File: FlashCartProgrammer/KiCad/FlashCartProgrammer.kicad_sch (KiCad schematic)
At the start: 85 parts, among them J1 Vic20 Cartridge Connector, J10 Vic20 Header, J11 ZIF Header, J2 C64 Cartridge Connector, J3 +5V, J4 USB_A_KeyBoard, J5 BOOT SEL, J6 VGA, J7 DM3D-SF, J8 SWD, J9 C64 Header, U1 TLV74311PDBVR, U10 27C400, U2 TLV74333PDBVR, U3 W25Q16JVSSIQ, U4 RP2350B-QFN80, U5 74LS573, U6 74LS573, U7 TXS0108EPW, U8 TXS0108EPW, U9 TXS0108EPW, Y1 12MHz

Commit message: - Cleaned up the Flash Cart Programmer PCB a bit.
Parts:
- removed C15: 4.7uf, Capacitor_SMD:C_0603_1608Metric, symbol Device:C_Small
- removed C31: 100nf, Capacitor_SMD:C_0603_1608Metric, symbol Device:C_Small
- removed J1: Vic20 Cartridge Connector, SamacSys_Parts:307044558201, symbol SamacSys_Parts:307-044-558-201
- removed J2: C64 Cartridge Connector, SamacSys_Parts:395044524202, symbol SamacSys_Parts:395-044-524-202
- removed J6: VGA, SamacSys_Parts:117345301, symbol Connector:DE15_Socket_HighDensity_MountingHoles
- removed U9: TXS0108EPW, Package_SO:TSSOP-20_4.4x6.5mm_P0.65mm, symbol Logic_LevelTranslator:TXS0108EPW
- added J1: Vic20_Cartridge_Connector, _Custom:Vic20-Cartridge-Connector, symbol _Custom:Vic20_Cartridge_Connector
- added J2: c64-Cartridge-Connector, _Custom:c64-Cartridge-Connector, symbol _Custom:c64-Cartridge-Connector
- added J6: DE15_Socket_HighDensity_MountingHoles, _Custom:DSUB-15, symbol _Custom:DE15_Socket_HighDensity_MountingHoles
- added R25, R26: 10k, Resistor_SMD:R_0603_1608Metric, symbol Device:R_Small
- added U18: 74LS245, Package_SO:TSSOP-20_4.4x6.5mm_P0.65mm, symbol Dave:74LVC245A
- C22, C23: value 8pf -> 12pf
- J11: footprint Connector_PinHeader_2.54mm:PinHeader_1x03_P2.54mm_Vertical -> Connector_PinHeader_2.54mm:PinHeader_1x04_P2.54mm_Vertical; symbol Connector:Conn_01x03_Pin -> Connector:Conn_01x04_Pin
- J4: footprint Connector_USB:USB_A_Connfly_DS1095 -> _Custom:USB_A
- R1, R2, R3, R4, R5, R7, R8, R9: value 27 -> 27R
- R10, R12, R14: value 340 -> 330R
- U10: footprint Socket:DIP_Socket-40_W11.9mm_W12.7mm_W15.24mm_W17.78mm_W18.5mm_3M_240-1280-00-0602J -> _Custom:ZIF-40_W11.9_W12.7_W15.24_W17.78_W18.5_3M_240-1280-00-0602J
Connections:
- net +3V3: no longer C30.2, R24.2
- net +5V: now also C30.2, J1.21 (5V), J2.2 (5V=), J2.3 (5V), U18.20 (VCC)
- net 3v3_A16: now also U18.18 (B0)
- net 3v3_A17: now also U18.17 (B1)
- net 3v3_A18: now also U18.16 (B2)
- net 3v3_A19: now also U18.15 (B3)
- net A0: now also J1.B (A0), J2.Y (A0)
- net A1: now also J1.C (A1), J2.X (A1)
- net A10: now also J1.N (A10), J2.M (A10)
- net A11: now also J1.P (A11), J2.L (A11)
- net A12: now also J1.R (A12), J2.K (A12)
- net A13: now also J2.11 (~{ROML})
- net A16: now also U18.2 (A0)
- net A17: now also U18.3 (A1)
- net A18: now also U18.4 (A2)
- net A19: now also U18.5 (A3)
- net A2: now also J1.D (A2), J2.W (A2)
- net A3: now also J1.E (A3), J2.V (A3)
- net A4: now also J1.F (A4), J2.U (A4)
- net A5: now also J1.H (A5), J2.T (A5)
- net A6: now also J1.J (A6), J2.S (A6)
- net A7: now also J1.K (A7), J2.R (A7)
- net A8: now also J1.L (A8), J2.P (A8)
- net A9: now also J1.M (A9), J2.N (A9)
- net D0: now also J1.2 (D0), J2.21 (D0)
- net D1: now also J1.3 (D1), J2.20 (D1)
- net D2: now also J1.4 (D2), J2.19 (D2)
- net D3: now also J1.5 (D3), J2.18 (D3)
- net D4: now also J1.6 (D4), J2.17 (D4)
- net D5: now also J1.7 (D5), J2.16 (D5)
- net D6: now also J1.8 (D6), J2.15 (D6)
- net D7: now also J1.9 (D7), J2.14 (D7)
- net GND: now also R24.2, J1.1 (GND1), J1.22 (GND2), J1.A (GND3), J1.Z (GND4), J2.0 (MH), J2.1 (GND1), J2.22 (GND2), J2.A (GND4), J2.Z (GND3), J6.10, J6.5, J6.6, J6.7, J6.8, J6.SH, R25.2, R26.1, U18.10 (GND)
- net VGA_BLUE: now also J6.3
- net VGA_GREEN: now also J6.2
- net VGA_H_SYNC: now also J6.13
- net VGA_RED: now also J6.1
- net VGA_V_SYNC: now also J6.14
- net ~{3v3_BYTE}: now also U18.14 (B4)
- net ~{3v3_OE}: now also U18.12 (B6)
- net ~{3v3_WE}: now also U18.13 (B5)
- net ~{BYTE}: now also U18.6 (A4)
- net ~{OE}: now also U18.8 (A6)
- net ~{WE}: now also U18.7 (A5)
- net at R4.1: now also J1.13 (~{BLK5})
- net at R24.1: now also U18.1 (A->B)
- net at R1.1: now also J1.10 (~{BLK1})
- net at R2.1: now also J1.11 (~{BLK2})
- net at R3.1: now also J1.12 (~{BLK3})
- net at R5.2: now also J2.B (~{ROMH})
- net SPI1.CS renamed SPI1.~{CS}
- net ~{3v3_CE} renamed ~{3v3_RESET}
- net ~{3v3_RESET}: now also U18.11 (B7)
- net ~{CE}: no longer names the net of U10.10 (~{CE})
- net ~{CE}: now also R26.2
- new net: R25.1, U18.19 (CE)
- new net ~{RESET}: J11.4 (Pin_4), U18.9 (A7)
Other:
- moved on the sheet: C24, C25, U5, U6

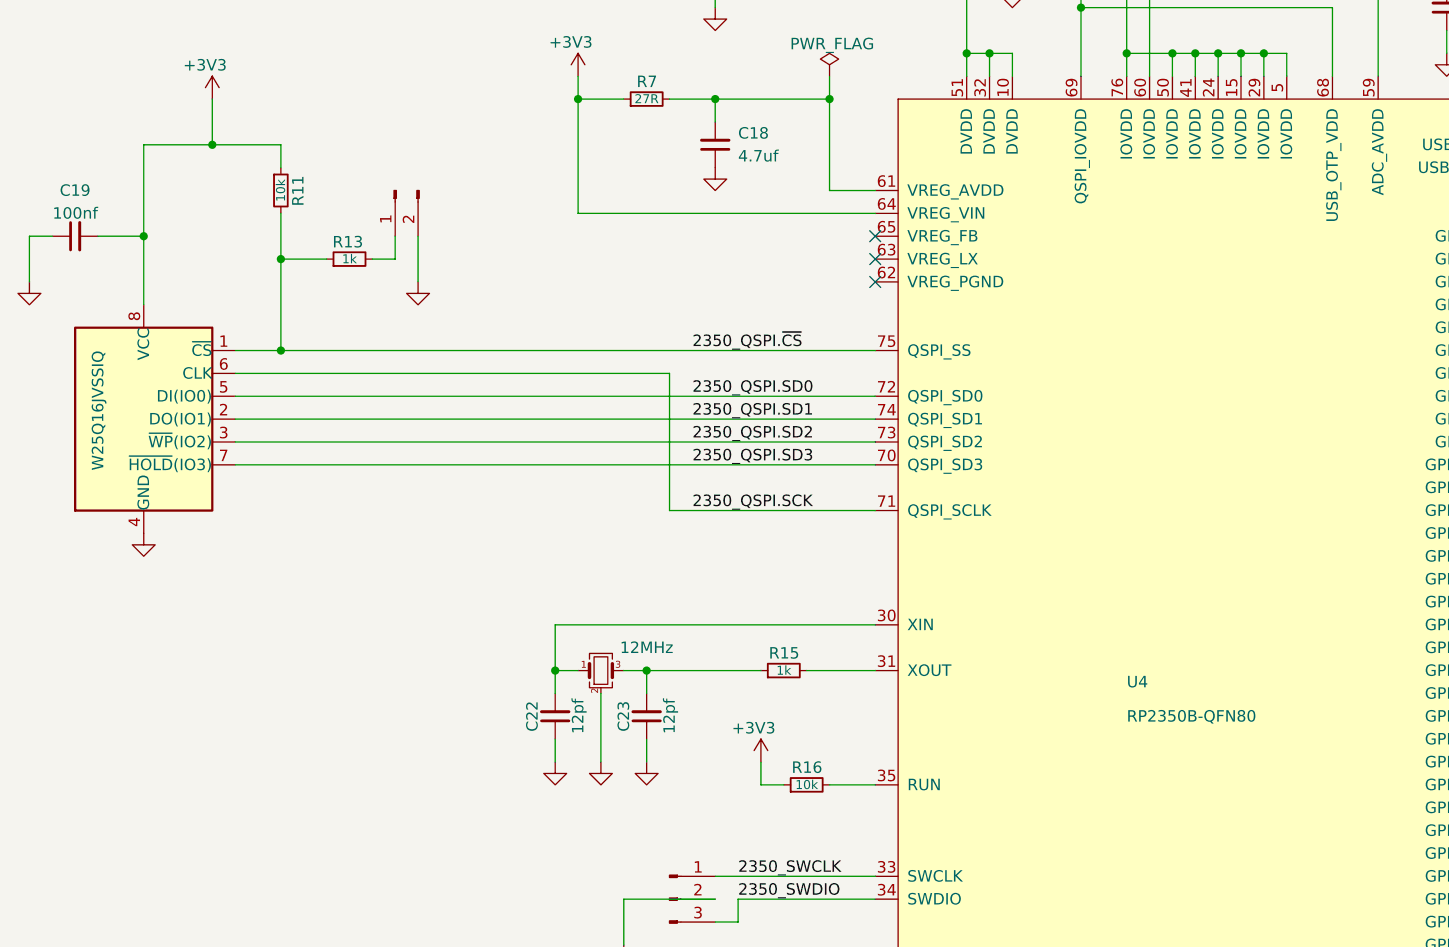
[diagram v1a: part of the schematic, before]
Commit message: - Removed references to my local parts.
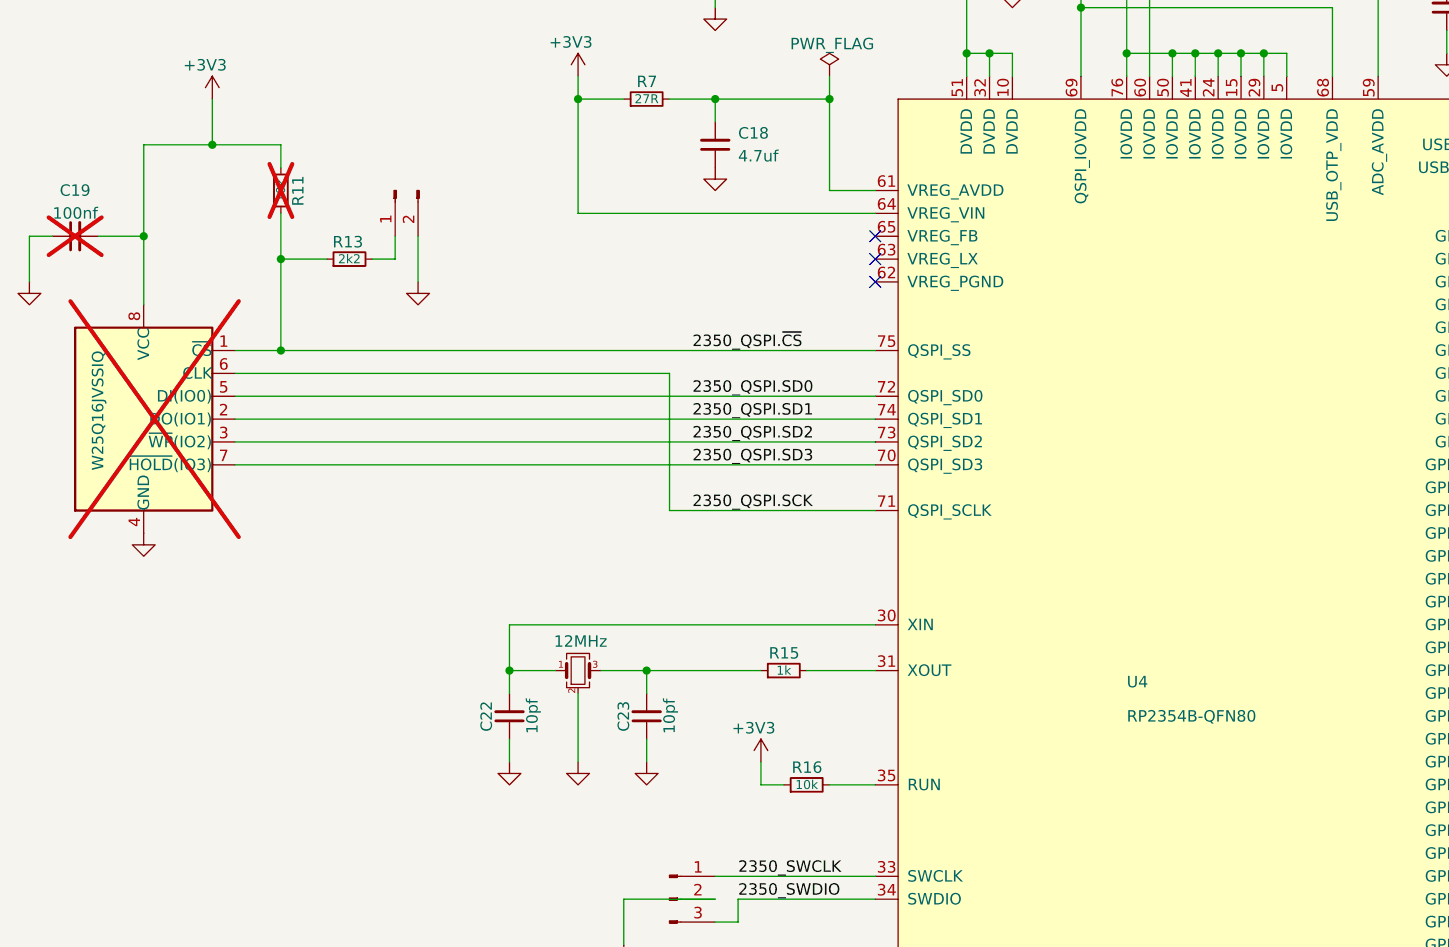
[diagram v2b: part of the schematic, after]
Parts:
- C19, R11: now not fitted
- C22, C23: value 12pf -> 10pf
- J7: footprint SamacSys_Parts:DM3DSF -> _Custom:DM3DSF_SDCard; symbol SamacSys_Parts:DM3D-SF -> _Custom:DM3D-SF_SDCard
- Power1: footprint SamacSys_Parts:LEDC2012X90N -> LED_SMD:LED_0805_2012Metric
- R13: value 1k -> 2k2
- U3: footprint Dave Footprints:SOIC-8_5.23x5.23mm_P1.27mm -> Package_SO:SOIC-8_5.3x5.3mm_P1.27mm; now not fitted
- U4: value RP2350B-QFN80 -> RP2354B-QFN80
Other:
- moved on the sheet: C22
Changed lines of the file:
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@@
 	)
 	(junction
-		(at 81.28 137.16)
+		(at 424.18 35.56)
 		(diameter 0)
 		(color 0 0 0 0)
 	)
 	(junction
-		(at 424.18 35.56)
+		(at 259.08 236.22)
 		(diameter 0)
 		(color 0 0 0 0)
 	)
 	(junction
-		(at 259.08 236.22)
+		(at 76.2 137.16)
 		(diameter 0)
 		(color 0 0 0 0)
@@
 	)
 	(junction
-		(at 91.44 137.16)
-		(diameter 0)
-		(color 0 0 0 0)
-	)
-	(junction
 		(at 530.86 73.66)
 		(diameter 0)
@@
 	)
 	(junction
+		(at 91.44 137.16)
+		(diameter 0)
+		(color 0 0 0 0)
+	)
+	(junction
 		(at 398.78 175.26)
 		(diameter 0)
@@
 	(wire
 		(pts
-			(xy 81.28 137.16) (xy 83.82 137.16)
+			(xy 76.2 137.16) (xy 81.28 137.16)
 		)
 		(stroke
@@
 	(wire
 		(pts
-			(xy 81.28 132.08) (xy 81.28 137.16)
+			(xy 76.2 132.08) (xy 76.2 137.16)
 		)
 		(stroke
@@
 	(wire
 		(pts
-			(xy 81.28 137.16) (xy 81.28 139.7)
+			(xy 76.2 137.16) (xy 76.2 139.7)
 		)
 		(stroke
@@
 	(wire
 		(pts
-			(xy 86.36 139.7) (xy 86.36 147.32)
+			(xy 83.82 139.7) (xy 83.82 147.32)
 		)
 		(stroke
@@
 	(wire
 		(pts
-			(xy 81.28 144.78) (xy 81.28 147.32)
+			(xy 76.2 144.78) (xy 76.2 147.32)
 		)
 		(stroke
@@
 	(wire
 		(pts
-			(xy 88.9 137.16) (xy 91.44 137.16)
+			(xy 86.36 137.16) (xy 91.44 137.16)
 		)
 		(stroke
@@
 	(wire
 		(pts
-			(xy 81.28 132.08) (xy 116.84 132.08)
+			(xy 76.2 132.08) (xy 116.84 132.08)
 		)
 		(stroke
@@
 			)
 		)
-		(property "Description" ""
+		(property "Description" "Unpolarized capacitor, small symbol"
 			(at 502.92 68.58 0)
 			(hide yes)
@@
 			)
 		)
-		(property "Description" ""
+		(property "Description" "Unpolarized capacitor, small symbol"
 			(at 213.36 38.1 0)
 			(hide yes)
@@
 			)
 		)
-		(property "Description" ""
+		(property "Description" "Unpolarized capacitor, small symbol"
 			(at 172.72 38.1 0)
 			(hide yes)
@@
 	(symbol
 		(lib_id "Device:C_Small")
-		(at 81.28 142.24 180)
+		(at 76.2 142.24 180)
 		(unit 1)
 		(body_style 1)
@@
 		(dnp no)
 		(property "Reference" "C22"
-			(at 78.74 142.24 90)
+			(at 73.66 142.24 90)
 			(show_name no)
 			(do_not_autoplace no)
@@
 			)
 		)
-		(property "Value" "12pf"
-			(at 83.82 142.24 90)
+		(property "Value" "10pf"
+			(at 78.74 142.24 90)
 			(show_name no)
 			(do_not_autoplace no)
@@
 		)
 		(property "Footprint" "Capacitor_SMD:C_0603_1608Metric"
-			(at 81.28 142.24 0)
+			(at 76.2 142.24 0)
 			(hide yes)
 			(show_name no)
@@
 		)
 		(property "Datasheet" ""
-			(at 81.28 142.24 0)
+			(at 76.2 142.24 0)
 			(hide yes)
 			(show_name no)
@@
 		)
 		(property "Description" "Unpolarized capacitor, small symbol"
-			(at 81.28 142.24 0)
+			(at 76.2 142.24 0)
 			(hide yes)
 			(show_name no)
@@
 			)
 		)
-		(property "Description" ""
+		(property "Description" "Unpolarized capacitor, small symbol"
 			(at 546.1 68.58 0)
 			(hide yes)
@@
 			)
 		)
-		(property "Value" "1k"
+		(property "Value" "2k2"
 			(at 58.42 91.44 90)
 			(show_name no)
@@
 	(symbol
 		(lib_id "power:GND")
-		(at 86.36 147.32 0)
+		(at 83.82 147.32 0)
 		(unit 1)
 		(body_style 1)
@@
 		(fields_autoplaced yes)
 		(property "Reference" "#PWR040"
-			(at 86.36 153.67 0)
+			(at 83.82 153.67 0)
 			(hide yes)
 			(show_name no)
@@
 		)
 		(property "Value" "GND"
-			(at 86.3599 151.13 90)
+			(at 83.8199 151.13 90)
 			(hide yes)
 			(show_name no)
@@
 		)
 		(property "Footprint" ""
-			(at 86.36 147.32 0)
+			(at 83.82 147.32 0)
 			(hide yes)
 			(show_name no)
@@
 		)
 		(property "Datasheet" ""
-			(at 86.36 147.32 0)
+			(at 83.82 147.32 0)
 			(hide yes)
 			(show_name no)
@@
 		)
 		(property "Description" "Power symbol creates a global label with name \"GND\" , ground"
-			(at 86.36 147.32 0)
+			(at 83.82 147.32 0)
 			(hide yes)
 			(show_name no)
@@
 			)
 		)
-		(property "Description" ""
+		(property "Description" "Unpolarized capacitor, small symbol"
 			(at 193.04 38.1 0)
 			(hide yes)
@@
 	)
 	(symbol
-		(lib_id "SamacSys_Parts:DM3D-SF")
+		(lib_id "_Custom:DM3D-SF_SDCard")
 		(at 325.12 139.7 0)
 		(unit 1)
@@
 			)
 		)
-		(property "Footprint" "SamacSys_Parts:DM3DSF"
+		(property "Footprint" "_Custom:DM3DSF_SDCard"
 			(at 354.33 234.62 0)
 			(hide yes)
@@
 		)
 		(property "Description" "Micro SD card push pull manual"
-			(at 325.12 139.7 0)
+			(at 325.12 175.26 0)
 			(hide yes)
 			(show_name no)
@@
 			)
 		)
-		(property "Description" ""
+		(property "Description" "Unpolarized capacitor, small symbol"
 			(at 180.34 63.5 0)
 			(hide yes)
@@
 			)
 		)
-		(property "Description" ""
+		(property "Description" "Unpolarized capacitor, small symbol"
 			(at 119.38 55.88 0)
 			(hide yes)
@@
 			)
 		)
-		(property "Description" ""
+		(property "Description" "Unpolarized capacitor, small symbol"
 			(at 109.22 55.88 0)
 			(hide yes)
@@
 			)
 		)
-		(property "Description" ""
+		(property "Description" "Unpolarized capacitor, small symbol"
 			(at 182.88 38.1 0)
 			(hide yes)
@@
 			)
 		)
-		(property "Description" ""
+		(property "Description" "Unpolarized capacitor, small symbol"
 			(at 99.06 78.74 0)
 			(hide yes)
@@
 		(on_board yes)
 		(in_pos_files yes)
-		(dnp no)
+		(dnp yes)
 		(property "Reference" "C19"
 			(at 27.94 83.82 90)
@@
 			)
 		)
-		(property "Value" "12pf"
+		(property "Value" "10pf"
 			(at 93.98 142.24 90)
 			(show_name no)
@@
 		(on_board yes)
 		(in_pos_files yes)
-		(dnp no)
+		(dnp yes)
 		(property "Reference" "U3"
 			(at 31.8632 97.3017 0)
@@
 			)
 		)
-		(property "Footprint" "Dave Footprints:SOIC-8_5.23x5.23mm_P1.27mm"
+		(property "Footprint" "Package_SO:SOIC-8_5.3x5.3mm_P1.27mm"
 			(at 34.798 138.43 0)
 			(hide yes)
@@
 	(symbol
 		(lib_id "power:GND")
-		(at 81.28 147.32 0)
+		(at 76.2 147.32 0)
 		(unit 1)
 		(body_style 1)
@@
 		(fields_autoplaced yes)
 		(property "Reference" "#PWR039"
-			(at 81.28 153.67 0)
+			(at 76.2 153.67 0)
 			(hide yes)
 			(show_name no)
@@
 		)
 		(property "Value" "GND"
-			(at 81.2799 151.13 90)
+			(at 76.1999 151.13 90)
 			(hide yes)
 			(show_name no)
@@
 		)
 		(property "Footprint" ""
-			(at 81.28 147.32 0)
+			(at 76.2 147.32 0)
 			(hide yes)
 			(show_name no)
@@
 		)
 		(property "Datasheet" ""
-			(at 81.28 147.32 0)
+			(at 76.2 147.32 0)
 			(hide yes)
 			(show_name no)
@@
 		)
 		(property "Description" "Power symbol creates a global label with name \"GND\" , ground"
-			(at 81.28 147.32 0)
+			(at 76.2 147.32 0)
 			(hide yes)
 			(show_name no)
@@
 	(symbol
 		(lib_id "Device:Crystal_GND24_Small")
-		(at 86.36 137.16 0)
+		(at 83.82 137.16 0)
 		(unit 1)
 		(body_style 1)
@@
 		(dnp no)
 		(property "Reference" "Y1"
-			(at 83.82 139.7 90)
+			(at 81.28 139.7 90)
 			(hide yes)
 			(show_name no)
@@
 		)
 		(property "Value" "12MHz"
-			(at 91.44 134.62 0)
+			(at 84.0989 133.9263 0)
 			(show_name no)
 			(do_not_autoplace no)
@@
 		)
 		(property "Footprint" "Crystal:Crystal_SMD_SeikoEpson_FA238V-4Pin_3.2x2.5mm"
-			(at 86.36 137.16 0)
+			(at 83.82 137.16 0)
 			(hide yes)
 			(show_name no)
@@
 		)
 		(property "Datasheet" ""
-			(at 86.36 137.16 0)
+			(at 83.82 137.16 0)
 			(hide yes)
 			(show_name no)
@@
 		)
 		(property "Description" "Four pin crystal, GND on pins 2 and 4, small symbol"
-			(at 86.36 137.16 0)
+			(at 83.82 137.16 0)
 			(hide yes)
 			(show_name no)
@@
 		)
 		(property "Note" ""
-			(at 86.36 137.16 0)
+			(at 83.82 137.16 0)
 			(hide yes)
 			(show_name no)
@@
 		)
 		(property "Voltage" ""
-			(at 86.36 137.16 0)
+			(at 83.82 137.16 0)
 			(hide yes)
 			(show_name no)
@@
 		)
 		(property "class" ""
-			(at 86.36 137.16 0)
+			(at 83.82 137.16 0)
 			(hide yes)
 			(show_name no)
@@
 			)
 		)
-		(property "Description" ""
+		(property "Description" "Unpolarized capacitor, small symbol"
 			(at 132.08 55.88 0)
 			(hide yes)
@@
 			)
 		)
-		(property "Description" ""
+		(property "Description" "Unpolarized capacitor, small symbol"
 			(at 99.06 55.88 0)
 			(hide yes)
@@
 		(on_board yes)
 		(in_pos_files yes)
-		(dnp no)
+		(dnp yes)
 		(property "Reference" "R11"
 			(at 52.7234 83.858 90)
@@
 			)
 		)
-		(property "Description" ""
+		(property "Description" "Unpolarized capacitor, small symbol"
 			(at 203.2 38.1 0)
 			(hide yes)
@@
 			)
 		)
-		(property "Footprint" "SamacSys_Parts:LEDC2012X90N"
+		(property "Footprint" "LED_SMD:LED_0805_2012Metric"
 			(at 431.8 53.34 0)
 			(hide yes)
@@
 			)
 		)
-		(property "Description" ""
+		(property "Description" "Unpolarized capacitor, small symbol"
 			(at 162.56 38.1 0)
 			(hide yes)
@@
 			)
 		)
-		(property "Description" ""
+		(property "Description" "Unpolarized capacitor, small symbol"
 			(at 152.4 38.1 0)
 			(hide yes)
@@
 			)
 		)
-		(property "Value" "RP2350B-QFN80"
+		(property "Value" "RP2354B-QFN80"
 			(at 144.78 142.24 0)
 			(show_name no)
